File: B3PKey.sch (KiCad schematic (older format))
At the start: 178 parts, among them SW1 SW_Push, U1 ATmega32U4-AU, Y1 16MHz

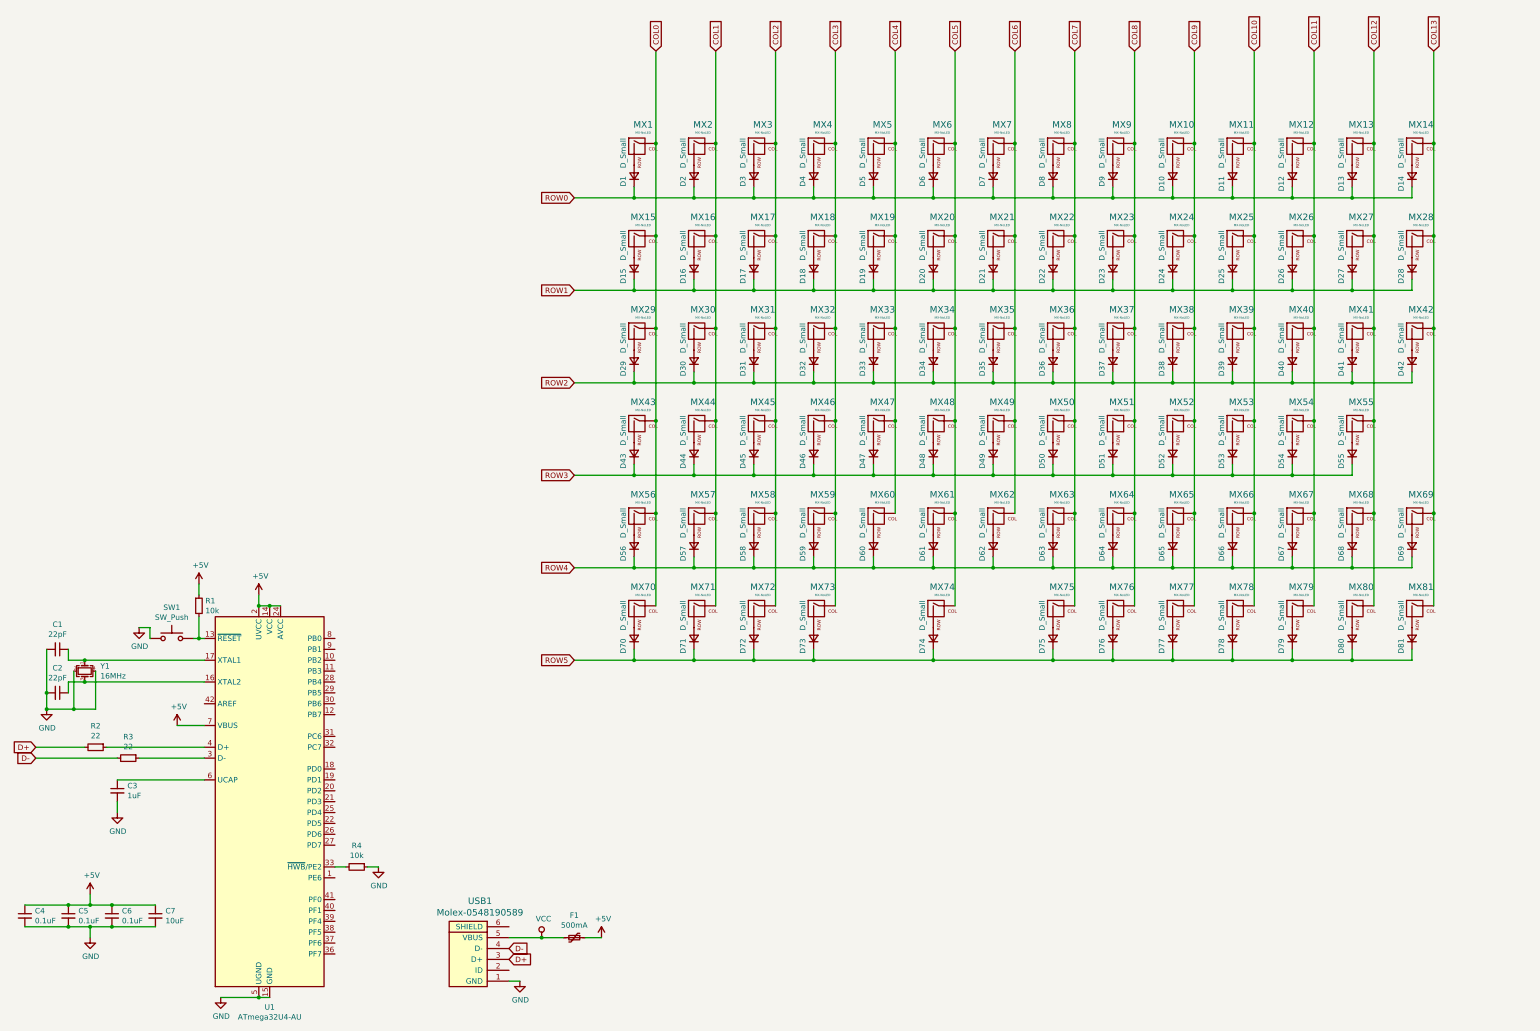
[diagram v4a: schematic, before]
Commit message: Update layout and replace microcontroller
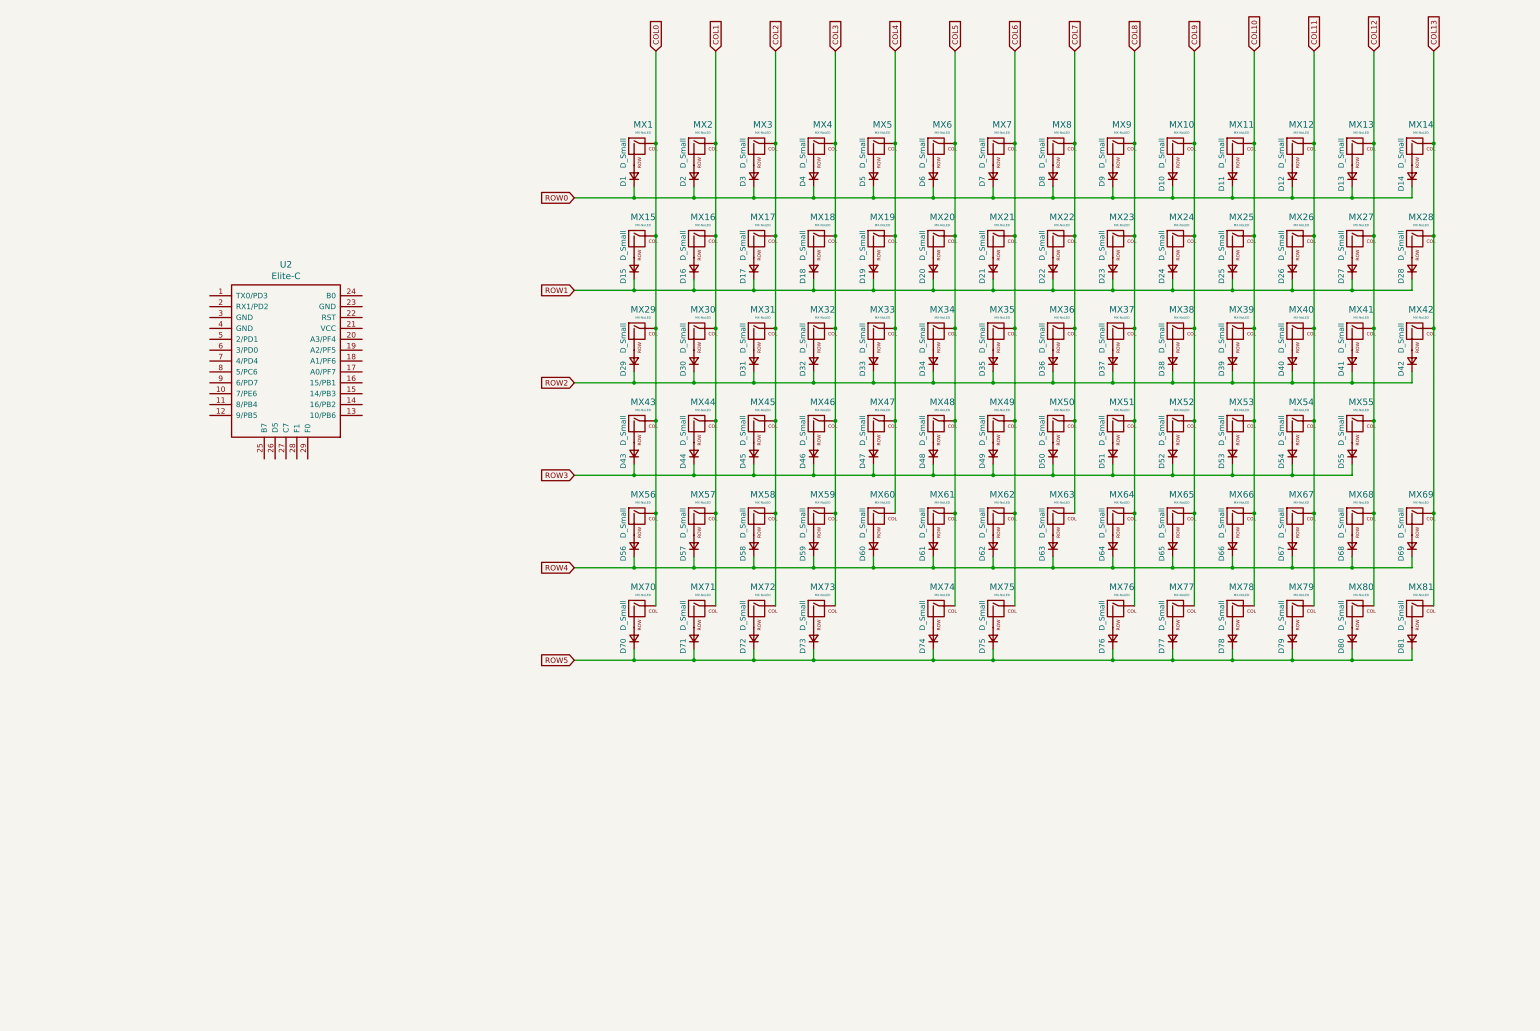
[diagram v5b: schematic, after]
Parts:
- removed C1, C2: 22pF, Capacitor_SMD:C_0805_2012Metric, symbol Device:C_Small
- removed C3: 1uF, Capacitor_SMD:C_0805_2012Metric, symbol Device:C_Small
- removed C4, C5, C6: 0.1uF, Capacitor_SMD:C_0805_2012Metric, symbol Device:C_Small
- removed C7: 10uF, Capacitor_SMD:C_0805_2012Metric, symbol Device:C_Small
- removed F1: 500mA, Fuse:Fuse_0805_2012Metric, symbol Device:Polyfuse_Small
- removed R1, R4: 10k, Resistor_SMD:R_0805_2012Metric, symbol Device:R_Small
- removed R2, R3: 22, Resistor_SMD:R_0805_2012Metric, symbol Device:R_Small
- removed SW1: SW_Push, random-keyboard-parts:SKQG-1155865, symbol Switch:SW_Push
- removed U1: ATmega32U4-AU, Package_QFP:TQFP-44_10x10mm_P0.8mm, symbol MCU_Microchip_ATmega:ATmega32U4-AU
- removed USB1: Molex-0548190589, random-keyboard-parts:Molex-0548190589, symbol random-keyboard-parts:Molex-0548190589
- removed Y1: 16MHz, Crystal:Crystal_SMD_3225-4Pin_3.2x2.5mm, symbol Device:Crystal_GND24_Small
- added U2: Elite-C, Keebio-Parts:Elite-C, symbol keebio:Elite-C
- MX74: footprint MX_Only:MXOnly-3U-ReversedStabilizers-NoLED -> MX_Only:MXOnly-2U-ReversedStabilizers-NoLED
- MX75: footprint MX_Only:MXOnly-1U-NoLED -> MX_Only:MXOnly-2U-ReversedStabilizers-NoLED
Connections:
- net COL6: now also MX75.1 (COL)
- net COL7: no longer MX75.1 (COL)
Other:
- moved on the sheet: D75, MX75
